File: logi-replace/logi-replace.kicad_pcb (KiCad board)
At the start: 2 copper layers, 34 parts, among them J7 USB_C_Receptacle_USB2.0_16P, U3 TPS7A26, Y2 12MHz

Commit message: HW: Started work on the amplifier stages
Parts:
- added C1: C, Capacitor_SMD:CP_Elec_4x4.5, F.Cu at (91.7, 108.8)
- added C10: C, Capacitor_SMD:CP_Elec_4x4.5, F.Cu at (259.8, 48.1)
- added C31: C, Capacitor_SMD:C_0603_1608Metric_Pad1.08x0.95mm_HandSolder, F.Cu at (91.5, 103.6)
- added C32: 1u, Capacitor_SMD:C_0402_1005Metric_Pad0.74x0.62mm_HandSolder, F.Cu at (187.5, 44.5)
- added C32: C, Capacitor_SMD:C_0603_1608Metric_Pad1.08x0.95mm_HandSolder, F.Cu at (239.4, 40.6)
- added C33: C, Capacitor_SMD:C_0603_1608Metric_Pad1.08x0.95mm_HandSolder, F.Cu at (93.4, 103.6)
- added C34: C, Capacitor_SMD:C_0603_1608Metric_Pad1.08x0.95mm_HandSolder, F.Cu at (95.3, 103.6)
- added C35: C, Capacitor_SMD:C_0603_1608Metric_Pad1.08x0.95mm_HandSolder, F.Cu at (104.7, 103.6)
- added C36: C, Capacitor_SMD:C_0603_1608Metric_Pad1.08x0.95mm_HandSolder, F.Cu at (106.6, 103.6)
- added C37: C, Capacitor_SMD:C_0402_1005Metric_Pad0.74x0.62mm_HandSolder, F.Cu at (187.5, 46.5)
- added C38: 220u, Capacitor_SMD:C_0402_1005Metric_Pad0.74x0.62mm_HandSolder, F.Cu at (187.5, 48.4)
- added C39: 220u, Capacitor_SMD:C_0402_1005Metric_Pad0.74x0.62mm_HandSolder, F.Cu at (187.5, 50.4)
- added C40: 220u, Capacitor_SMD:C_0402_1005Metric_Pad0.74x0.62mm_HandSolder, F.Cu at (187.5, 52.4)
- added C41: 220u, Capacitor_SMD:C_0402_1005Metric_Pad0.74x0.62mm_HandSolder, F.Cu at (187.5, 54.3)
- added C42: 680n, Capacitor_SMD:C_0603_1608Metric_Pad1.08x0.95mm_HandSolder, F.Cu at (204.0, 74.2)
- added C43: 680n, Capacitor_SMD:C_0603_1608Metric_Pad1.08x0.95mm_HandSolder, F.Cu at (204.0, 76.7)
- added C44: 1n, Capacitor_SMD:C_0603_1608Metric_Pad1.08x0.95mm_HandSolder, F.Cu at (204.0, 79.2)
- added C45: 1n, Capacitor_SMD:C_0603_1608Metric_Pad1.08x0.95mm_HandSolder, F.Cu at (204.0, 81.7)
- added C46: 10n, Capacitor_SMD:C_0603_1608Metric_Pad1.08x0.95mm_HandSolder, F.Cu at (208.3, 74.2)
- added C47: 10n, Capacitor_SMD:C_0603_1608Metric_Pad1.08x0.95mm_HandSolder, F.Cu at (208.3, 76.7)
- added C48: 680n, Capacitor_SMD:C_0603_1608Metric_Pad1.08x0.95mm_HandSolder, F.Cu at (208.3, 79.2)
- added C49: 680n, Capacitor_SMD:C_0603_1608Metric_Pad1.08x0.95mm_HandSolder, F.Cu at (208.3, 81.7)
- added C50: 1n, Capacitor_SMD:C_0603_1608Metric_Pad1.08x0.95mm_HandSolder, F.Cu at (212.7, 74.2)
- added C51: 1n, Capacitor_SMD:C_0603_1608Metric_Pad1.08x0.95mm_HandSolder, F.Cu at (212.7, 76.7)
- added C52: 10n, Capacitor_SMD:C_0603_1608Metric_Pad1.08x0.95mm_HandSolder, F.Cu at (212.7, 79.2)
- added C53: 10n, Capacitor_SMD:C_0603_1608Metric_Pad1.08x0.95mm_HandSolder, F.Cu at (212.7, 81.7)
- added C54: C, Capacitor_SMD:C_0603_1608Metric_Pad1.08x0.95mm_HandSolder, F.Cu at (239.4, 43.1)
- added C55: C, Capacitor_SMD:C_0603_1608Metric_Pad1.08x0.95mm_HandSolder, F.Cu at (239.4, 45.6)
- added C56: 220u, Capacitor_SMD:C_0402_1005Metric_Pad0.74x0.62mm_HandSolder, F.Cu at (247.5, 52.9)
- added C57: 220u, Capacitor_SMD:C_0402_1005Metric_Pad0.74x0.62mm_HandSolder, F.Cu at (247.5, 54.9)
- added C58: C, Capacitor_SMD:C_0603_1608Metric_Pad1.08x0.95mm_HandSolder, F.Cu at (239.4, 48.1)
- added C59: 1u, Capacitor_SMD:C_0603_1608Metric_Pad1.08x0.95mm_HandSolder, F.Cu at (239.4, 50.6)
- added C6: C, Capacitor_SMD:CP_Elec_4x4.5, F.Cu at (108.3, 108.7)
- added C60: 1u, Capacitor_SMD:C_0603_1608Metric_Pad1.08x0.95mm_HandSolder, F.Cu at (239.4, 53.1)
- added C61: C, Capacitor_SMD:C_0603_1608Metric_Pad1.08x0.95mm_HandSolder, F.Cu at (243.7, 40.6)
- added C62: 1n, Capacitor_SMD:C_0603_1608Metric_Pad1.08x0.95mm_HandSolder, F.Cu at (243.7, 43.1)
- added C63: 1n, Capacitor_SMD:C_0603_1608Metric_Pad1.08x0.95mm_HandSolder, F.Cu at (243.7, 45.6)
- added C64: 10n, Capacitor_SMD:C_0603_1608Metric_Pad1.08x0.95mm_HandSolder, F.Cu at (243.7, 48.1)
- added C65: 10n, Capacitor_SMD:C_0603_1608Metric_Pad1.08x0.95mm_HandSolder, F.Cu at (243.7, 50.6)
- added C66: C, Capacitor_SMD:C_0402_1005Metric_Pad0.74x0.62mm_HandSolder, F.Cu at (247.5, 56.9)
- added C67: 220u, Capacitor_SMD:C_0402_1005Metric_Pad0.74x0.62mm_HandSolder, F.Cu at (247.5, 58.8)
- added C68: 220u, Capacitor_SMD:C_0402_1005Metric_Pad0.74x0.62mm_HandSolder, F.Cu at (247.5, 60.8)
- added C9: C, Capacitor_SMD:CP_Elec_4x4.5, F.Cu at (259.8, 42.2)
- added H1: MountingHole_Pad, MountingHole:MountingHole_3.2mm_M3_Pad, F.Cu at (68.0, 47.0)
- added H2: MountingHole_Pad, MountingHole:MountingHole_3.2mm_M3_Pad, F.Cu at (132.8, 47.6)
- added H3: MountingHole_Pad, MountingHole:MountingHole_3.2mm_M3_Pad, F.Cu at (67.0, 153.5)
- added H4: MountingHole_Pad, MountingHole:MountingHole_3.2mm_M3_Pad, F.Cu at (133.0, 152.1)
- added LOUT1: RCA, library:REAN_Black, F.Cu at (120.0, 60.0)
- added R20: 27k, Resistor_SMD:R_0402_1005Metric_Pad0.72x0.64mm_HandSolder, F.Cu at (173.1, 57.1)
- added R21: R, Resistor_SMD:R_0402_1005Metric_Pad0.72x0.64mm_HandSolder, F.Cu at (173.1, 59.1)
- added R22: 5k1, Resistor_SMD:R_0402_1005Metric_Pad0.72x0.64mm_HandSolder, F.Cu at (173.1, 61.1)
- added R23: 5k1, Resistor_SMD:R_0402_1005Metric_Pad0.72x0.64mm_HandSolder, F.Cu at (173.1, 63.1)
- added R30: 5k1, Resistor_SMD:R_0402_1005Metric_Pad0.72x0.64mm_HandSolder, F.Cu at (176.4, 57.1)
- added R30: R, Resistor_SMD:R_0402_1005Metric_Pad0.72x0.64mm_HandSolder, F.Cu at (250.8, 52.9)
- added R31: 5k1, Resistor_SMD:R_0402_1005Metric_Pad0.72x0.64mm_HandSolder, F.Cu at (176.4, 59.1)
- added R32: 5k1, Resistor_SMD:R_0402_1005Metric_Pad0.72x0.64mm_HandSolder, F.Cu at (176.4, 61.1)
- added R33: 5k1, Resistor_SMD:R_0402_1005Metric_Pad0.72x0.64mm_HandSolder, F.Cu at (176.4, 63.1)
- added R34: 5k1, Resistor_SMD:R_0402_1005Metric_Pad0.72x0.64mm_HandSolder, F.Cu at (179.7, 57.1)
- added R35: 5k1, Resistor_SMD:R_0402_1005Metric_Pad0.72x0.64mm_HandSolder, F.Cu at (179.7, 59.1)
- added R36: 10k, Resistor_SMD:R_0402_1005Metric_Pad0.72x0.64mm_HandSolder, F.Cu at (203.4, 85.9)
- added R37: 20k, Resistor_SMD:R_0402_1005Metric_Pad0.72x0.64mm_HandSolder, F.Cu at (179.7, 61.1)
- added R38: 100k, Resistor_SMD:R_0402_1005Metric_Pad0.72x0.64mm_HandSolder, F.Cu at (179.7, 63.1)
- added R39: 3R3, Resistor_SMD:R_0402_1005Metric_Pad0.72x0.64mm_HandSolder, F.Cu at (216.5, 73.9)
- added R40: 3R3, Resistor_SMD:R_0402_1005Metric_Pad0.72x0.64mm_HandSolder, F.Cu at (216.5, 75.9)
- added R41: 3R3, Resistor_SMD:R_0402_1005Metric_Pad0.72x0.64mm_HandSolder, F.Cu at (216.5, 77.9)
- added R42: 3R3, Resistor_SMD:R_0402_1005Metric_Pad0.72x0.64mm_HandSolder, F.Cu at (216.5, 79.9)
- added R43: 3R3, Resistor_SMD:R_0402_1005Metric_Pad0.72x0.64mm_HandSolder, F.Cu at (250.8, 54.9)
- added R44: 3R3, Resistor_SMD:R_0402_1005Metric_Pad0.72x0.64mm_HandSolder, F.Cu at (250.8, 56.9)
- added R45: 47k, Resistor_SMD:R_0402_1005Metric_Pad0.72x0.64mm_HandSolder, F.Cu at (250.8, 58.9)
- added R46: 75k, Resistor_SMD:R_0402_1005Metric_Pad0.72x0.64mm_HandSolder, F.Cu at (254.0, 52.9)
- added R47: 5k1, Resistor_SMD:R_0402_1005Metric_Pad0.72x0.64mm_HandSolder, F.Cu at (254.0, 54.9)
- added R48: R, Resistor_SMD:R_0402_1005Metric_Pad0.72x0.64mm_HandSolder, F.Cu at (254.0, 56.9)
- added R49: 5k1, Resistor_SMD:R_0402_1005Metric_Pad0.72x0.64mm_HandSolder, F.Cu at (254.0, 58.9)
- added R50: R, Resistor_SMD:R_0402_1005Metric_Pad0.72x0.64mm_HandSolder, F.Cu at (257.3, 52.9)
- added R51: 5k1, Resistor_SMD:R_0402_1005Metric_Pad0.72x0.64mm_HandSolder, F.Cu at (257.3, 54.9)
- added R52: R, Resistor_SMD:R_0402_1005Metric_Pad0.72x0.64mm_HandSolder, F.Cu at (257.3, 56.9)
- added R53: 5k1, Resistor_SMD:R_0402_1005Metric_Pad0.72x0.64mm_HandSolder, F.Cu at (257.3, 58.9)
- added ROUT1: RCA, library:REAN_Red, F.Cu at (80.0, 60.0)
- added U1: TPA311xD2-Q1, Package_SO:HTSSOP-32-1EP_6.1x11mm_P0.65mm_EP5.2x11mm_Mask4.11x4.36mm_ThermalVias, F.Cu at (100.0, 110.0)
- added U4: TPA311xD2-Q1, Package_SO:HTSSOP-32-1EP_6.1x11mm_P0.65mm_EP5.2x11mm_Mask4.11x4.36mm_ThermalVias, F.Cu at (250.9, 45.6)
- added U5: NE5532, Package_SO:SOIC-8_3.9x4.9mm_P1.27mm, F.Cu at (243.7, 89.5)
- added U6: NE5532, Package_SO:SOIC-8_3.9x4.9mm_P1.27mm, F.Cu at (243.7, 96.0)
- added U7: NE5532, Package_SO:SOIC-8_3.9x4.9mm_P1.27mm, F.Cu at (254.2, 89.5)
- added U8: NE5532, Package_SO:SOIC-8_3.9x4.9mm_P1.27mm, F.Cu at (254.2, 96.0)
- moved R27 139.9 mm to (203.4, 56.4)
- moved J7 139.9 mm to (210.5, 47.2)
- moved R26 139.9 mm to (203.4, 54.4)
- moved C24 132.8 mm to (196.1, 62.1)
- moved C23 132.7 mm to (196.1, 60.2)
- moved C20 129.8 mm to (192.9, 66.1), turned to 0 degrees
- moved Y2 129.6 mm to (210.3, 53.0), turned to 0 degrees
- moved C19 129.5 mm to (192.9, 64.1), turned to 0 degrees
- moved C15 129.4 mm to (192.9, 56.2), turned to 0 degrees
- moved R18 126.8 mm to (203.4, 46.5), turned to 0 degrees
- moved U2 126.4 mm to (196.5, 49.4)
- moved C27 122.1 mm to (199.4, 56.2)
- moved C28 122.1 mm to (199.4, 58.2)
- moved C21 118.9 mm to (196.1, 56.2)
- moved C25 118.7 mm to (196.1, 64.1), turned to 0 degrees
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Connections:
- net /Amplifier1/IN_L renamed /Audio/OUT_L
- net /Amplifier1/IN_R renamed /Audio/OUT_R
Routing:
- net VDDI: track 13.8 -> 0.00 mm
- net /Audio/XTI: track 10.2 -> 0.00 mm
- net /Audio/XTO: track 7.34 -> 0.00 mm
- net VBUS1: track 7.00 -> 0.00 mm, vias 2 -> 0
- net /Audio/VCCP1I: track 3.19 -> 0.00 mm
- net /Audio/VCCP2I: track 3.07 -> 0.00 mm
- net /Audio/VCOM: track 3.07 -> 0.00 mm
- net /Audio/VOUTR: track 3.04 -> 0.00 mm
- net /Audio/VOUTL: track 3.03 -> 0.00 mm
- net /Amp LR/OUTNR: track 0.00 -> 3.00 mm
- net /Amp LR/BSNR: track 0.00 -> 2.97 mm
- net /Audio/VINL: track 2.90 -> 0.00 mm
- net /Audio/VINR: track 2.89 -> 0.00 mm
- net /Audio/VCCCI: track 2.81 -> 0.00 mm
- net /Audio/DM: track 2.73 -> 0.00 mm
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- added copper zone on F.Cu, net +24VA
- added copper zone on B.Cu, net GND
- removed copper zone on F.Cu, net /Audio/OUT
- removed copper zone on F.Cu, net /Audio/PG
- removed copper zone on F.Cu, net VBUS1
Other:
- board outline added: 80 x 120 mm

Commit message: HW: Set board outlone and hole constraints
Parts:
- added H10: MountingHole_Pad, MountingHole:MountingHole_3.2mm_M3_Pad, F.Cu at (125.0, 128.8)
- added H5: MountingHole_Pad, MountingHole:MountingHole_3.2mm_M3_Pad, F.Cu at (125.0, 31.0)
- added H6: MountingHole_Pad, MountingHole:MountingHole_3.2mm_M3_Pad, F.Cu at (75.0, 128.8)
- added H7: MountingHole_Pad, MountingHole:MountingHole_3.2mm_M3_Pad, F.Cu at (100.0, 188.0)
- added H8: MountingHole_Pad, MountingHole:MountingHole_3.2mm_M3_Pad, F.Cu at (75.0, 179.0)
- added H9: MountingHole_Pad, MountingHole:MountingHole_3.2mm_M3_Pad, F.Cu at (125.0, 179.0)
- C10: footprint Capacitor_SMD:CP_Elec_4x4.5 -> Capacitor_SMD:C_0603_1608Metric_Pad1.08x0.95mm_HandSolder
- C15, C16, C17, C18, C19, C20, C21, C22, C23, C24, C25, C26, C27, C28, C29, C30, C37, C38, C39, C40, C41, C56, C57, C66, C67, C68: footprint Capacitor_SMD:C_0402_1005Metric_Pad0.74x0.62mm_HandSolder -> Capacitor_SMD:C_0603_1608Metric_Pad1.08x0.95mm_HandSolder
- R17, R18, R19, R21, R22, R23, R24, R25, R26, R27, R28, R29, R30, R31, R32, R33, R34, R35, R36, R37, R38, R39, R40, R41, R42, R43, R44, R45, R46, R47, R48, R49, R50, R51, R52, R53: footprint Resistor_SMD:R_0402_1005Metric_Pad0.72x0.64mm_HandSolder -> Resistor_SMD:R_0603_1608Metric_Pad0.98x0.95mm_HandSolder
- moved R39 132.5 mm to (84.8, 59.4), turned to 180 degrees
- moved R40 129.3 mm to (88.3, 59.4), turned to 180 degrees
- moved C46 126.8 mm to (82.3, 60.3), turned to -90 degrees
- moved C44 120.5 mm to (84.8, 61.0), turned to 180 degrees
- moved C42 119.7 mm to (84.8, 62.6), turned to 180 degrees
- moved C47 118.7 mm to (90.8, 60.2), turned to 90 degrees
- moved C45 117.6 mm to (88.2, 61.0), turned to 180 degrees
- moved C43 116.6 mm to (88.2, 62.6), turned to 180 degrees
- moved R41 113.2 mm to (104.8, 59.4), turned to 180 degrees
- moved C52 112.2 mm to (102.1, 60.3), turned to -90 degrees
- moved C38 110.6 mm to (96.2, 110.9), turned to -90 degrees
- moved R42 110.1 mm to (108.3, 59.4), turned to 180 degrees
- moved C50 108.6 mm to (104.8, 61.0), turned to 180 degrees
- moved C40 105.9 mm to (99.3, 110.9), turned to -90 degrees
- moved C51 105.6 mm to (108.3, 61.0), turned to 180 degrees
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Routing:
- net GND: track 0.00 -> 23.5 mm
- net /Amp LR/OUTPR: track 0.00 -> 3.75 mm
- net /Amp LR/BSNL: track 0.00 -> 3.25 mm
- net /Amp LR/OUTNL: track 0.00 -> 3.05 mm
- net /Amp LR/OUTPL: track 0.00 -> 2.55 mm
- net /Amp LR/BSPL: track 0.00 -> 2.50 mm
- net /Amp LR/BSPR: track 0.00 -> 1.76 mm
- net /Amp LR/BSNR: track 2.97 -> 1.78 mm
- net /Amp LR/OUTNR: track 3.00 -> 3.78 mm
- added copper zone on F.Cu, net /Amp LR/OUTL_N
- added copper zone on F.Cu, net /Amp LR/OUTL_P
- added copper zone on F.Cu, net /Amp LR/OUTR_N
- added copper zone on F.Cu, net /Amp LR/OUTR_P
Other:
- board size 80 x 120 mm -> 60 x 174 mm

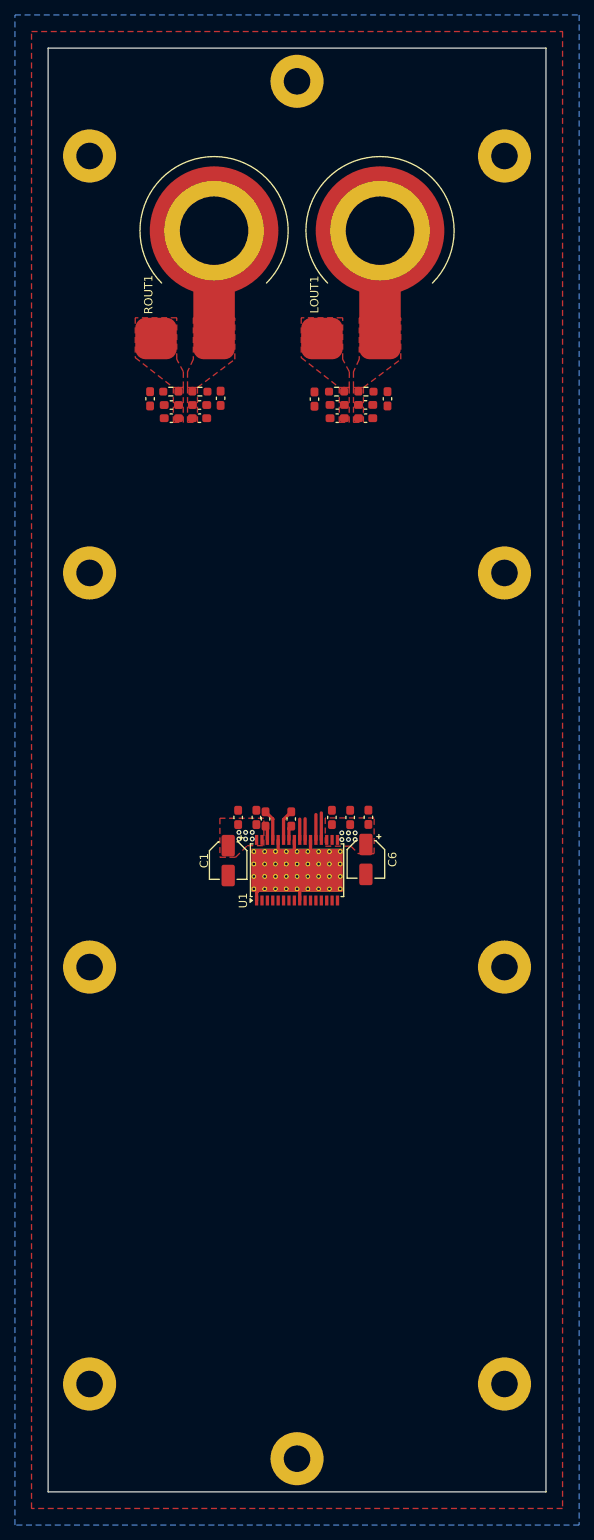
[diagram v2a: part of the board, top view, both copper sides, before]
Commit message: HW: Add via fencing on all non-curved outer edges
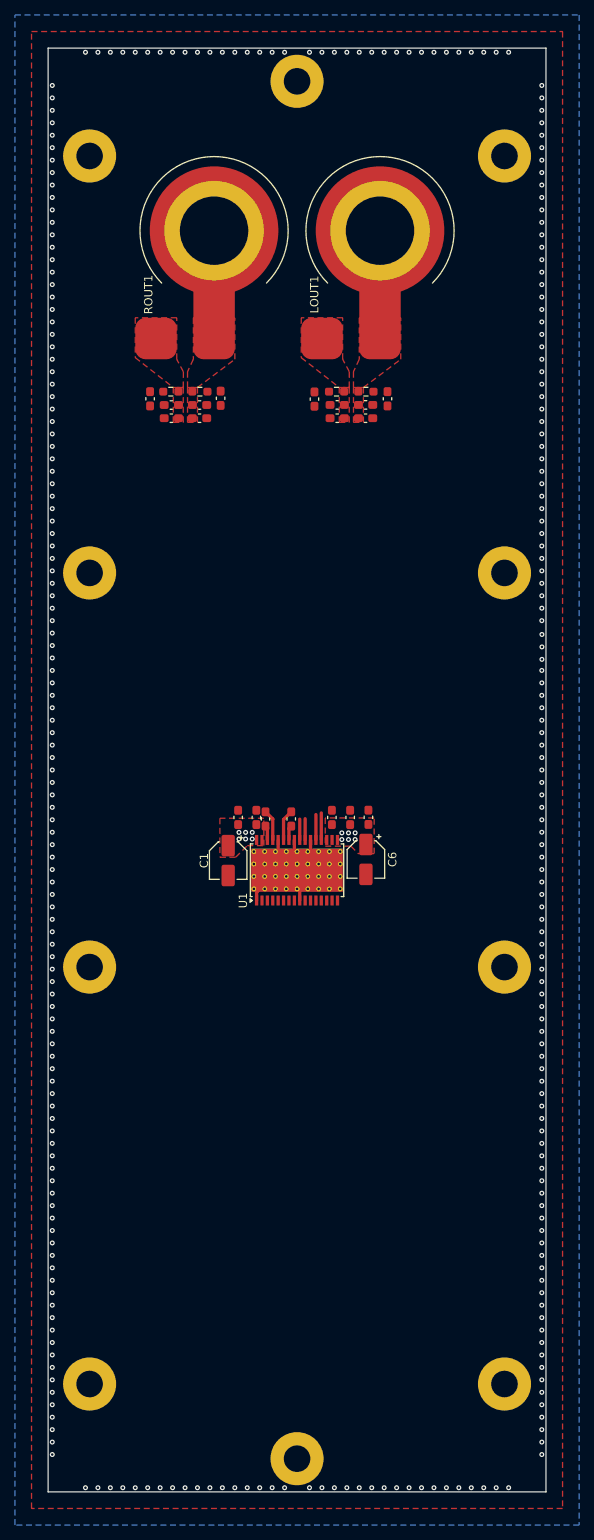
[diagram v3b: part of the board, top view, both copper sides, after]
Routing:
- net GND: vias 0 -> 290
